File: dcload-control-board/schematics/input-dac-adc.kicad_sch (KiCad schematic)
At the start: 30 parts, among them J300 Conn_01x02_Female, U300 INA159, U301 INA159, U302 TMUX1119, U303 AD7091R

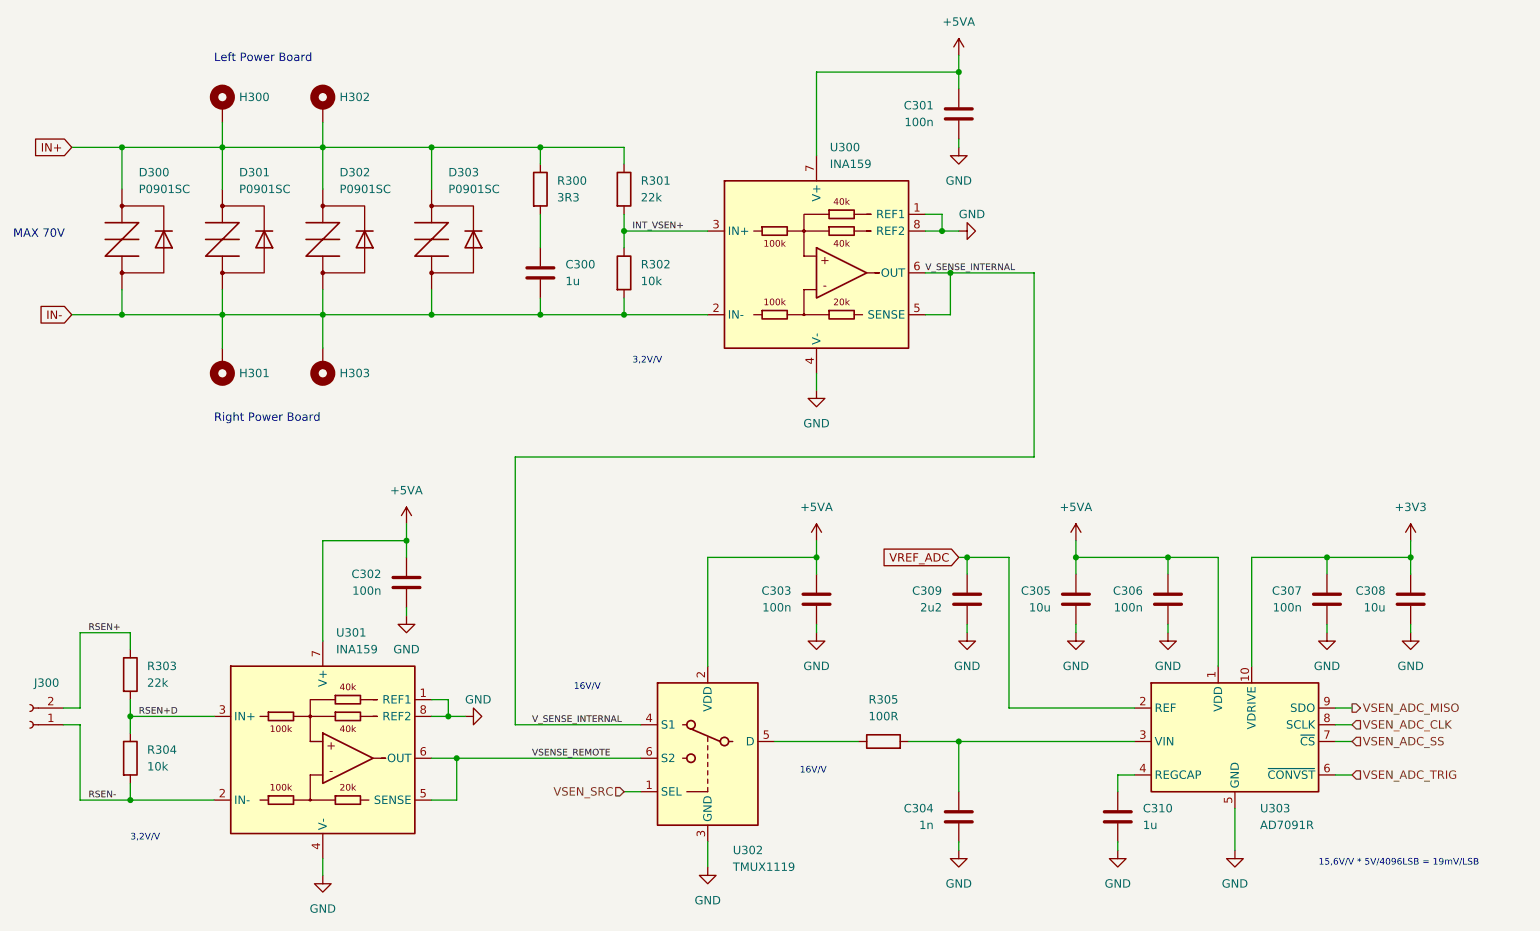
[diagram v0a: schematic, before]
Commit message: add: interface panel board
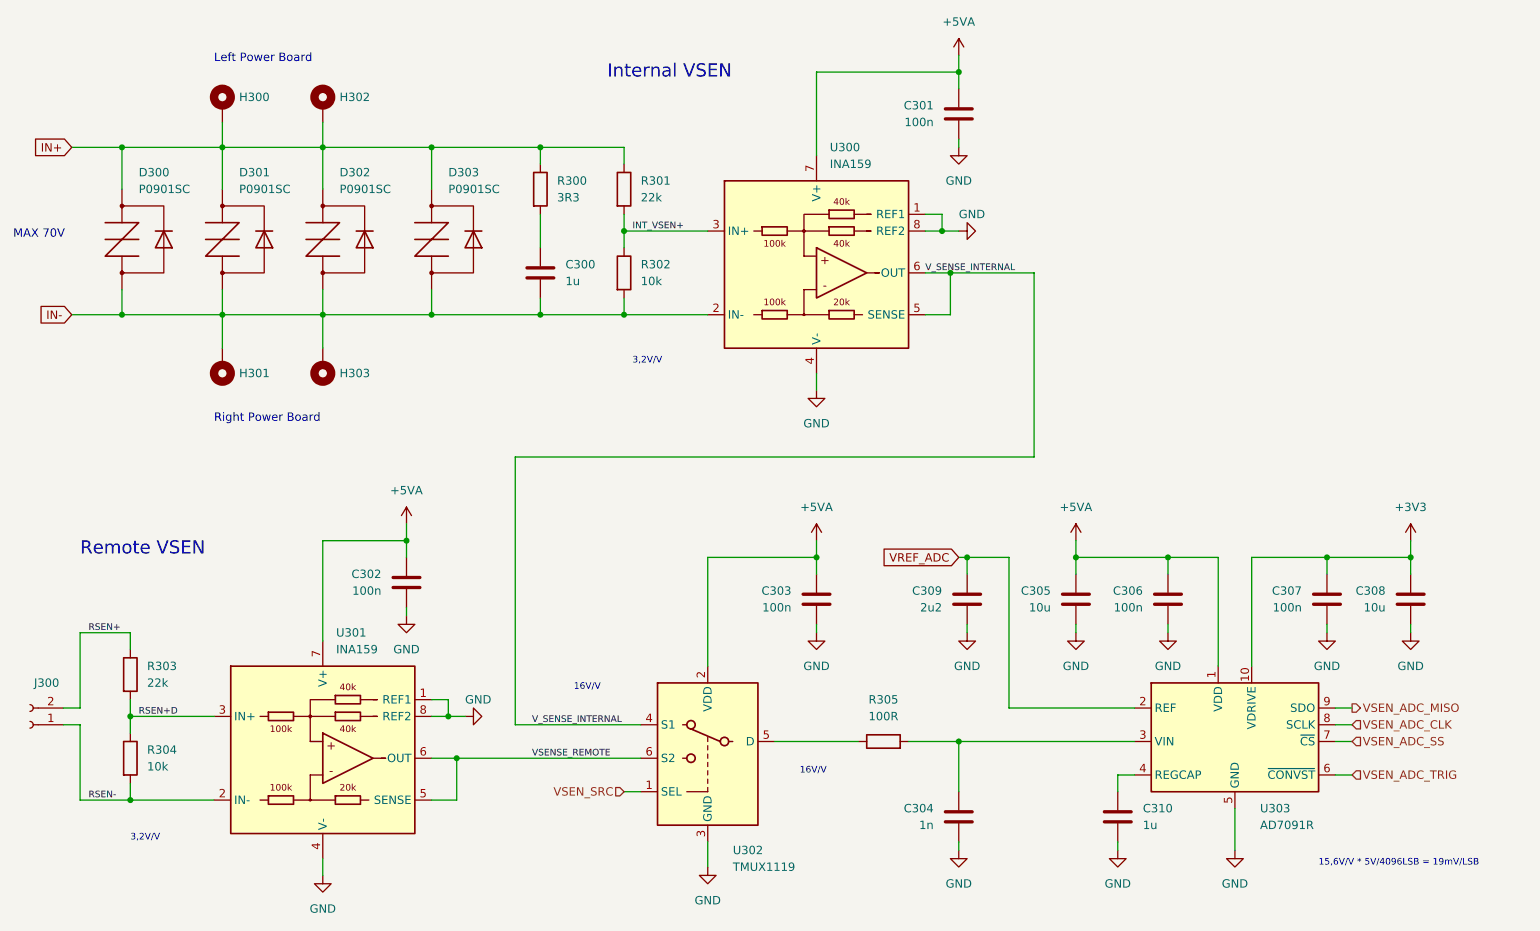
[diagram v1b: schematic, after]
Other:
- note added: "Internal VSEN"
- note added: "Remote VSEN"
- company: (none) -> Martin Kopka
- title: (none) -> Input Protection & Voltage Sense
